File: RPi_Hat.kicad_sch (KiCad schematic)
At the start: 16 parts, among them IC1 0.96_I2C_OLED, IC4 0.96_I2C_OLED, J1 RPi_GPIO, J2 TCBM, SW1 Select, SW2 Up, SW3 Down, SW4 Exit, SW5 Add Disk

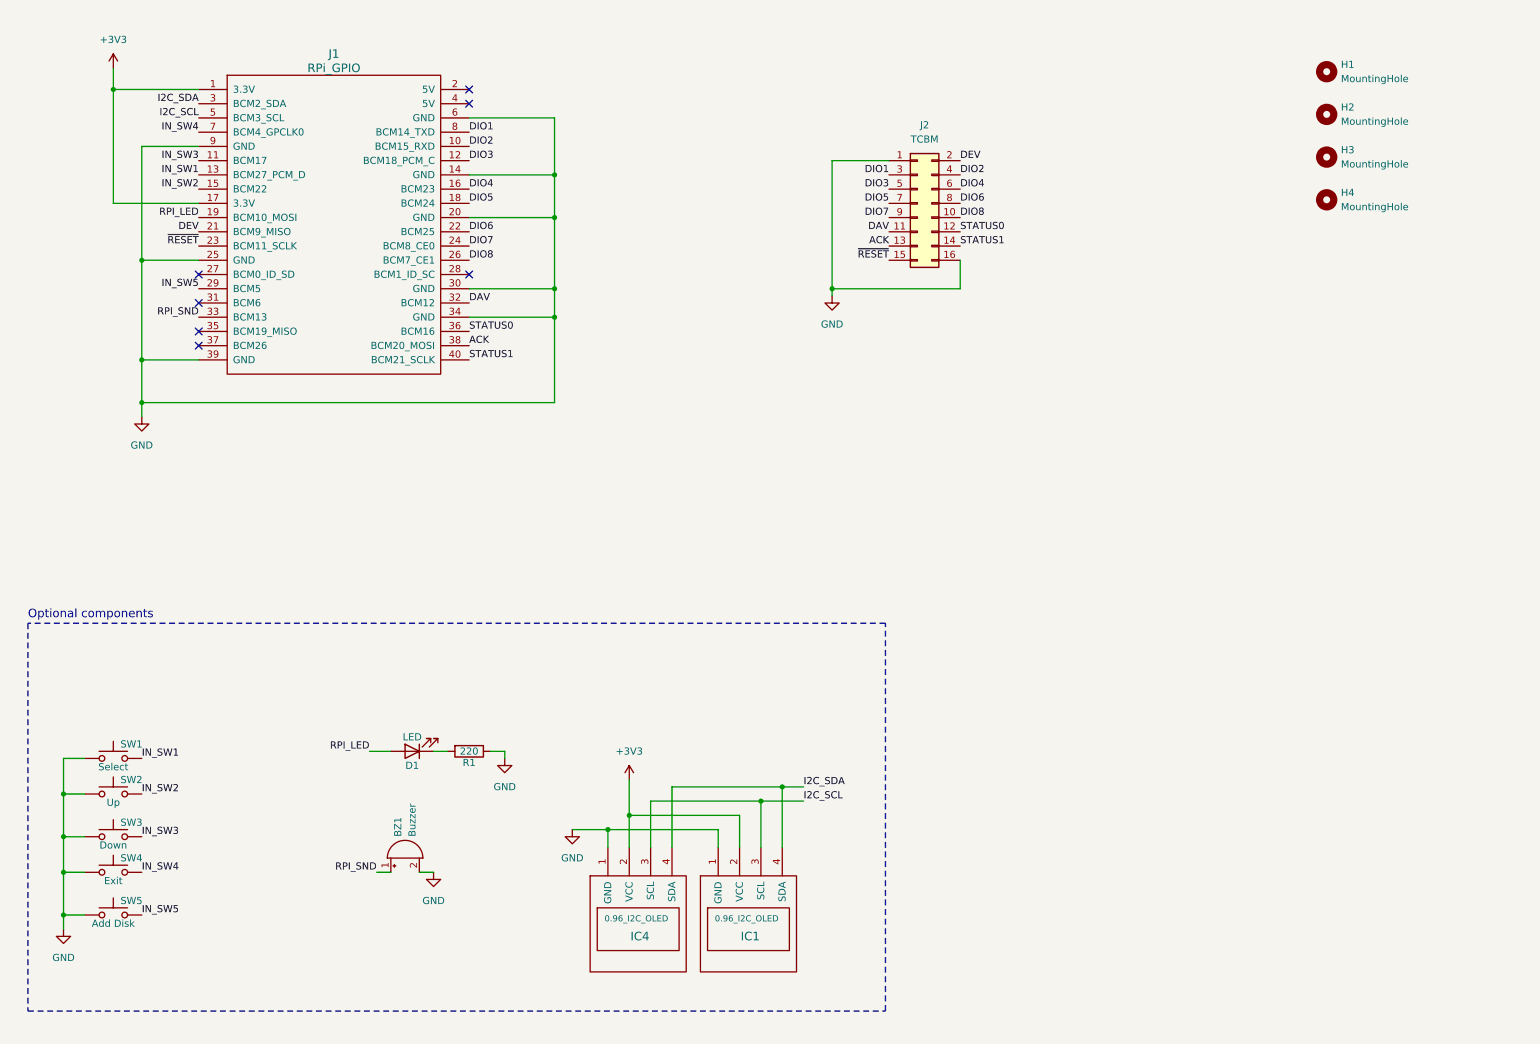
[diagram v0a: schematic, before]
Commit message: /RESET voltage level protection, connector for rotary encoder, tape connector support
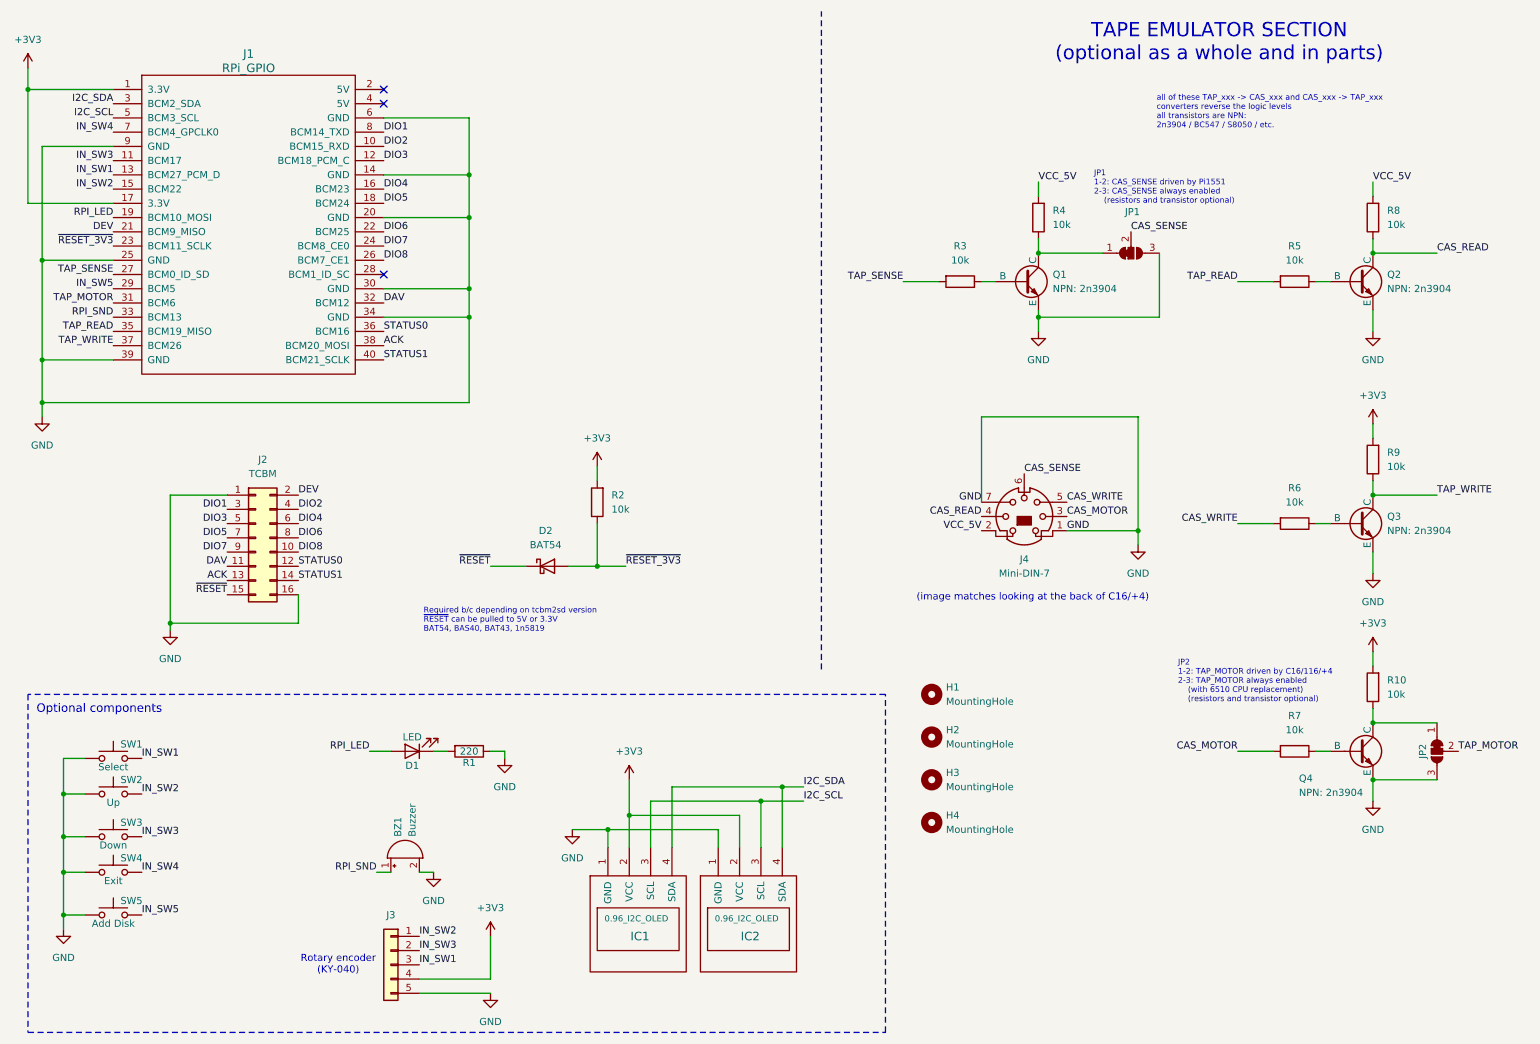
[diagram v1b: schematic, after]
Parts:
- added D2: BAT54, Diode_THT:D_A-405_P7.62mm_Horizontal, symbol Device:D_Schottky
- added J3: Conn_01x05, Connector_PinHeader_2.54mm:PinHeader_1x05_P2.54mm_Vertical, symbol Connector_Generic:Conn_01x05
- added J4: Mini-DIN-7, Connector_PinHeader_2.54mm:PinHeader_1x07_P2.54mm_Vertical, symbol Connector:Mini-DIN-7
- added JP1, JP2: SolderJumper_3_Bridged12, Jumper:SolderJumper-3_P1.3mm_Bridged12_RoundedPad1.0x1.5mm_NumberLabels, symbol Jumper:SolderJumper_3_Bridged12
- added Q1, Q2, Q3, Q4: NPN: 2n3904, symbol Simulation_SPICE:NPN
- added R10, R2, R3, R4, R5, R6, R7, R8, R9: 10k, Resistor_THT:R_Axial_DIN0207_L6.3mm_D2.5mm_P10.16mm_Horizontal, symbol Device:R
- renumbered IC4 to IC1, IC1 to IC2
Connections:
- net +3V3: now also J3.4 (Pin_4), R10.2, R2.2, R9.2
- net GND: now also J3.5 (Pin_5), J4.1, J4.7, JP1.3 (B), JP2.3 (B), Q1.3 (E), Q2.3 (E), Q3.3 (E), Q4.3 (E)
- net IN_SW1: now also J3.3 (Pin_3)
- net IN_SW2: now also J3.1 (Pin_1)
- net IN_SW3: now also J3.2 (Pin_2)
- net ~{RESET}: now also D2.1 (K); no longer J1.23 (BCM11_SCLK)
- net TAP_SENSE: now reaches J1.27 (BCM0_ID_SD)
- net TAP_SENSE: now also R3.2
- net TAP_MOTOR: now reaches J1.31 (BCM6)
- net TAP_MOTOR: now also JP2.2 (C)
- net TAP_READ: now reaches J1.35 (BCM19_MISO)
- net TAP_READ: now also R5.2
- net TAP_WRITE: now reaches J1.37 (BCM26)
- net TAP_WRITE: now also Q3.1 (C), R9.1
- new net: JP1.1 (A), Q1.1 (C), R4.1
- new net: Q2.2 (B), R5.1
- new net: JP2.1 (A), Q4.1 (C), R10.1
- new net: Q4.2 (B), R7.1
- new net: Q3.2 (B), R6.1
- new net: Q1.2 (B), R3.1
- new net CAS_MOTOR: J4.3, R7.2
- new net CAS_READ: J4.4, Q2.1 (C), R8.1
- new net CAS_SENSE: J4.6, JP1.2 (C)
- new net CAS_WRITE: J4.5, R6.2
- new net VCC_5V: J4.2, R4.2, R8.2
- new net ~{RESET_3V3}: D2.2 (A), J1.23 (BCM11_SCLK), R2.1
- no-connect marks 7 -> 3
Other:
- note added: "(image matches looking at the back of C16/+4)"
- note added: "JP1 1-2: CAS_SENSE driven by Pi1551 2-3: CAS_SENSE always enabled (resistors and transistor optional)"
- note added: "JP2 1-2: TAP_MOTOR driven by C16/116/+4 2-3: TAP_MOTOR always enabled (with 6510 CPU replacement) (resistors and transistor optional)"
- note added: "Required b/c depending on tcbm2sd version ~{RESET} can be pulled to 5V or 3.3V BAT54, BAS40, BAT43, 1n5819"
- note added: "Rotary encoder (KY-040)"
- note added: "TAPE EMULATOR SECTION (optional as a whole and in parts)"
- note added: "all of these TAP_xxx -> CAS_xxx and CAS_xxx -> TAP_xxx converters reverse the logic levels all transistors are NPN: 2n3904 / BC547 / S8050 / etc."
- moved on the sheet: H1, H2, H3, H4, J1, J2

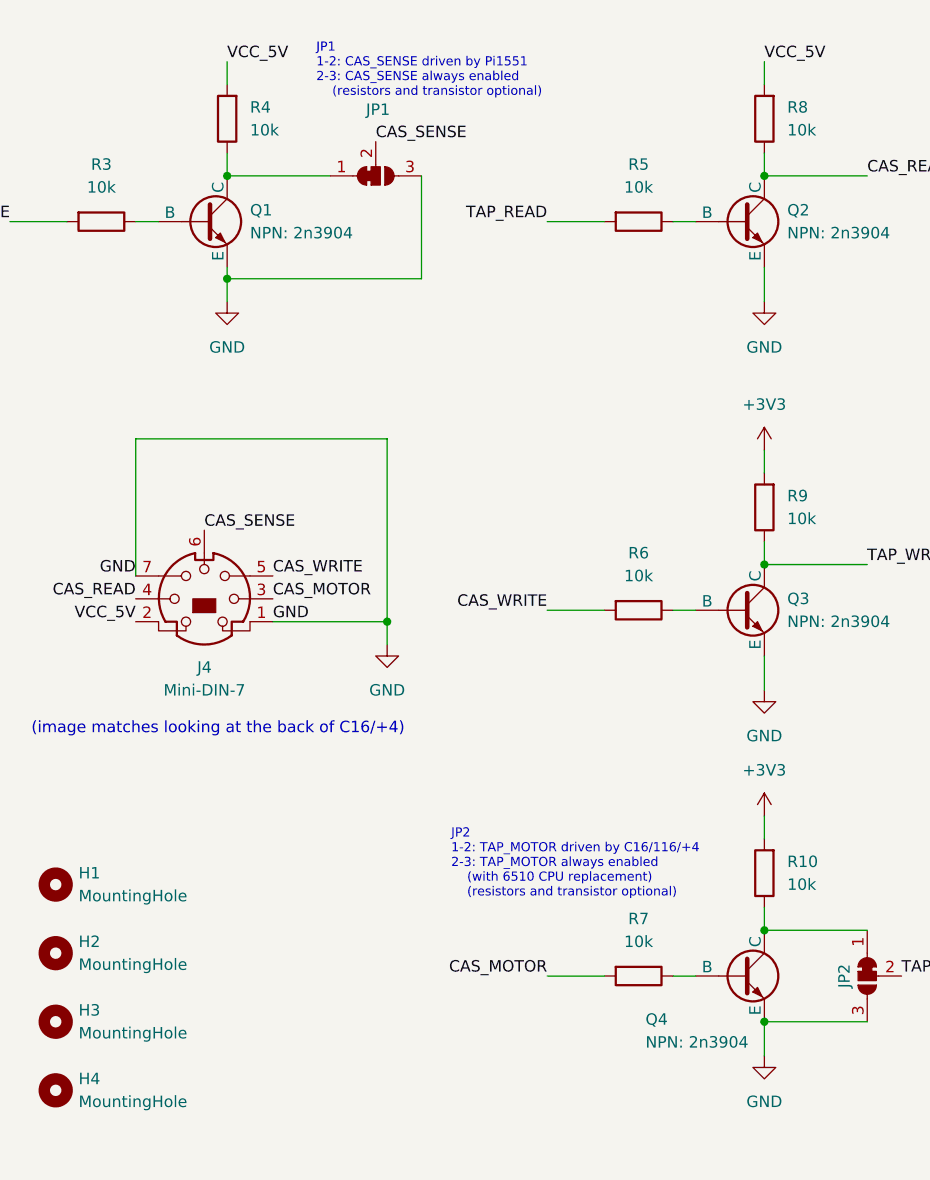
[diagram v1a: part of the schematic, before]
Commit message: completed tht version with tape interface support
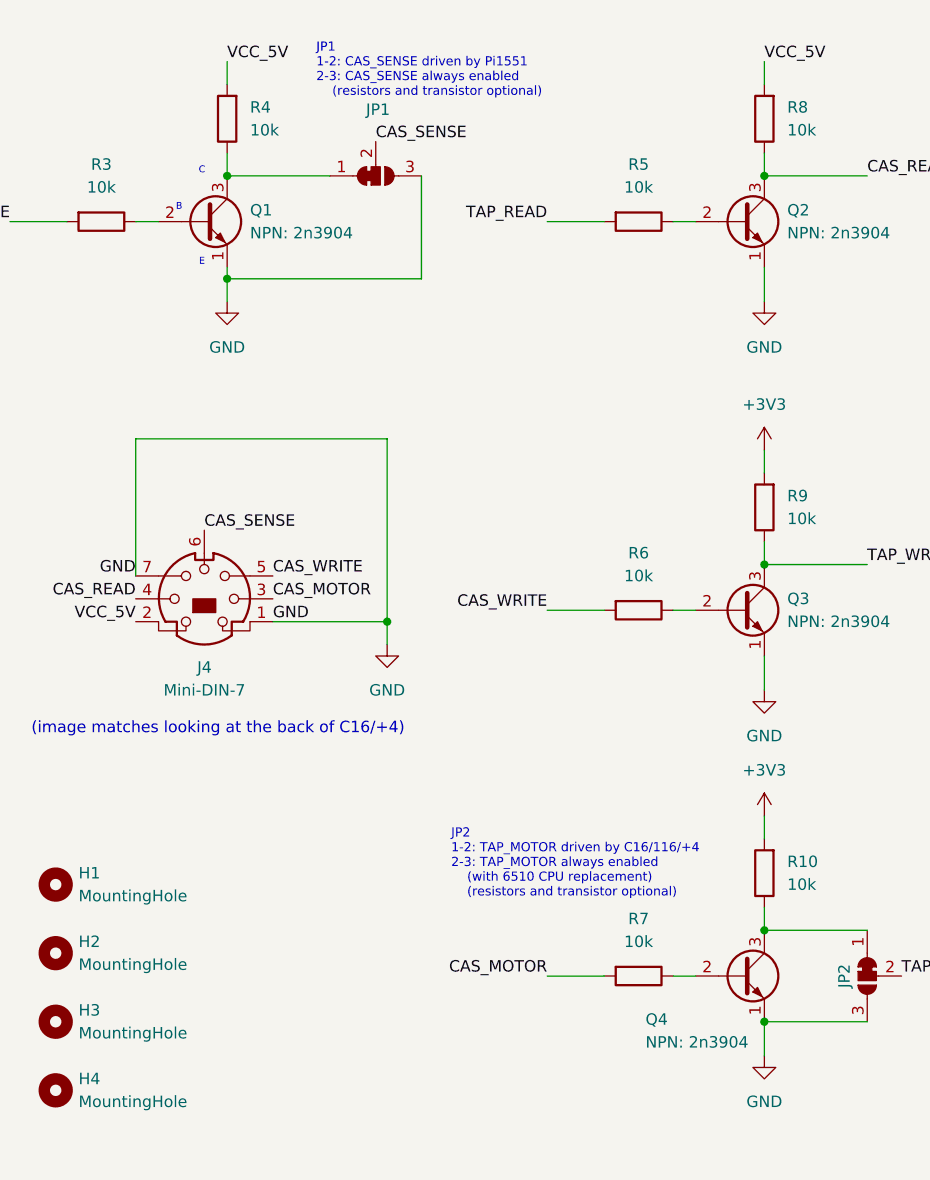
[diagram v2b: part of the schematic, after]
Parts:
- Q1, Q2, Q3, Q4: footprint (none) -> Package_TO_SOT_THT:TO-92_Inline; symbol Simulation_SPICE:NPN -> Transistor_BJT:2N3904
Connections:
- net CAS_READ: now also Q2.3 (C); no longer Q2.1 (C)
- net GND: now also Q1.1 (E), Q2.1 (E), Q3.1 (E), Q4.1 (E); no longer Q1.3 (E), Q2.3 (E), Q3.3 (E), Q4.3 (E)
- net TAP_WRITE: now also Q3.3 (C); no longer Q3.1 (C)
- net at JP1.1 (A), R4.1: now also Q1.3 (C); no longer Q1.1 (C)
- net at JP2.1 (A), R10.1: now also Q4.3 (C); no longer Q4.1 (C)
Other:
- note added: "B"
- note added: "C"
- note added: "E"
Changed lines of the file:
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@@
 		)
 	)
+	(text "C"
+		(exclude_from_sim no)
+		(at 194.056 57.912 0)
+		(effects
+			(font
+				(size 0.762 0.762)
+			)
+		)
+	)
 	(text "JP1\n1-2: CAS_SENSE driven by Pi1551\n2-3: CAS_SENSE always enabled\n    (resistors and transistor optional)"
 		(exclude_from_sim no)
@@
 		)
 	)
+	(text "B"
+		(exclude_from_sim no)
+		(at 191.516 61.976 0)
+		(effects
+			(font
+				(size 0.762 0.762)
+			)
+		)
+	)
 	(text "(image matches looking at the back of C16/+4)"
 		(exclude_from_sim no)
@@
 		)
 	)
+	(text "E"
+		(exclude_from_sim no)
+		(at 194.056 68.072 0)
+		(effects
+			(font
+				(size 0.762 0.762)
+			)
+		)
+	)
 	(text "Required b/c depending on tcbm2sd version\n~{RESET} can be pulled to 5V or 3.3V\nBAT54, BAS40, BAT43, 1n5819"
 		(exclude_from_sim no)
@@
 	)
 	(symbol
-		(lib_id "Simulation_SPICE:NPN")
+		(lib_id "Transistor_BJT:2N3904")
 		(at 254 63.5 0)
 		(unit 1)
@@
 			)
 		)
-		(property "Footprint" ""
-			(at 317.5 63.5 0)
+		(property "Footprint" "Package_TO_SOT_THT:TO-92_Inline"
+			(at 259.08 65.405 0)
 			(effects
 				(font
 					(size 1.27 1.27)
+					(italic yes)
 				)
+				(justify left)
 				(hide yes)
 			)
 		)
-		(property "Datasheet" "https://ngspice.sourceforge.io/docs/ngspice-html-manual/manual.xhtml#cha_BJTs"
-			(at 317.5 63.5 0)
+		(property "Datasheet" "https://www.onsemi.com/pub/Collateral/2N3903-D.PDF"
+			(at 254 63.5 0)
 			(effects
 				(font
 					(size 1.27 1.27)
 				)
+				(justify left)
 				(hide yes)
 			)
 		)
-		(property "Description" "Bipolar transistor symbol for simulation only, substrate tied to the emitter"
+		(property "Description" "0.2A Ic, 40V Vce, Small Signal NPN Transistor, TO-92"
 			(at 254 63.5 0)
 			(effects
@@
 	)
 	(symbol
-		(lib_id "Simulation_SPICE:NPN")
+		(lib_id "Transistor_BJT:2N3904")
 		(at 254 147.32 0)
 		(unit 1)
@@
 			)
 		)
-		(property "Footprint" ""
-			(at 317.5 147.32 0)
+		(property "Footprint" "Package_TO_SOT_THT:TO-92_Inline"
+			(at 259.08 149.225 0)
 			(effects
 				(font
 					(size 1.27 1.27)
+					(italic yes)
 				)
+				(justify left)
 				(hide yes)
 			)
 		)
-		(property "Datasheet" "https://ngspice.sourceforge.io/docs/ngspice-html-manual/manual.xhtml#cha_BJTs"
-			(at 317.5 147.32 0)
+		(property "Datasheet" "https://www.onsemi.com/pub/Collateral/2N3903-D.PDF"
+			(at 254 147.32 0)
 			(effects
 				(font
 					(size 1.27 1.27)
 				)
+				(justify left)
 				(hide yes)
 			)
 		)
-		(property "Description" "Bipolar transistor symbol for simulation only, substrate tied to the emitter"
+		(property "Description" "0.2A Ic, 40V Vce, Small Signal NPN Transistor, TO-92"
 			(at 254 147.32 0)
 			(effects
@@
 	)
 	(symbol
-		(lib_id "Simulation_SPICE:NPN")
+		(lib_id "Transistor_BJT:2N3904")
 		(at 254 106.68 0)
 		(unit 1)
@@
 			)
 		)
-		(property "Footprint" ""
-			(at 317.5 106.68 0)
+		(property "Footprint" "Package_TO_SOT_THT:TO-92_Inline"
+			(at 259.08 108.585 0)
 			(effects
 				(font
 					(size 1.27 1.27)
+					(italic yes)
 				)
+				(justify left)
 				(hide yes)
 			)
 		)
-		(property "Datasheet" "https://ngspice.sourceforge.io/docs/ngspice-html-manual/manual.xhtml#cha_BJTs"
-			(at 317.5 106.68 0)
+		(property "Datasheet" "https://www.onsemi.com/pub/Collateral/2N3903-D.PDF"
+			(at 254 106.68 0)
 			(effects
 				(font
 					(size 1.27 1.27)
 				)
+				(justify left)
 				(hide yes)
 			)
 		)
-		(property "Description" "Bipolar transistor symbol for simulation only, substrate tied to the emitter"
+		(property "Description" "0.2A Ic, 40V Vce, Small Signal NPN Transistor, TO-92"
 			(at 254 106.68 0)
 			(effects
@@
 	)
 	(symbol
-		(lib_id "Simulation_SPICE:NPN")
+		(lib_id "Transistor_BJT:2N3904")
 		(at 194.31 63.5 0)
 		(unit 1)
@@
 			)
 		)
-		(property "Footprint" ""
-			(at 257.81 63.5 0)
+		(property "Footprint" "Package_TO_SOT_THT:TO-92_Inline"
+			(at 199.39 65.405 0)
 			(effects
 				(font
 					(size 1.27 1.27)
+					(italic yes)
 				)
+				(justify left)
 				(hide yes)
 			)
 		)
-		(property "Datasheet" "https://ngspice.sourceforge.io/docs/ngspice-html-manual/manual.xhtml#cha_BJTs"
-			(at 257.81 63.5 0)
+		(property "Datasheet" "https://www.onsemi.com/pub/Collateral/2N3903-D.PDF"
+			(at 194.31 63.5 0)
 			(effects
 				(font
 					(size 1.27 1.27)
 				)
+				(justify left)
 				(hide yes)
 			)
 		)
-		(property "Description" "Bipolar transistor symbol for simulation only, substrate tied to the emitter"
+		(property "Description" "0.2A Ic, 40V Vce, Small Signal NPN Transistor, TO-92"
 			(at 194.31 63.5 0)
 			(effects
